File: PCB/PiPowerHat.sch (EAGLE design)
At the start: 48 parts, among them J3 Display, J4 FAN1, K1 PIN20X2, Q1 NX2301P, U1 EEPROM24, U2 INA219AIDCNRSOIC, U3 TSL2561T, U4 DS18B20, U5 DS1820SOIC, U6 74AC125

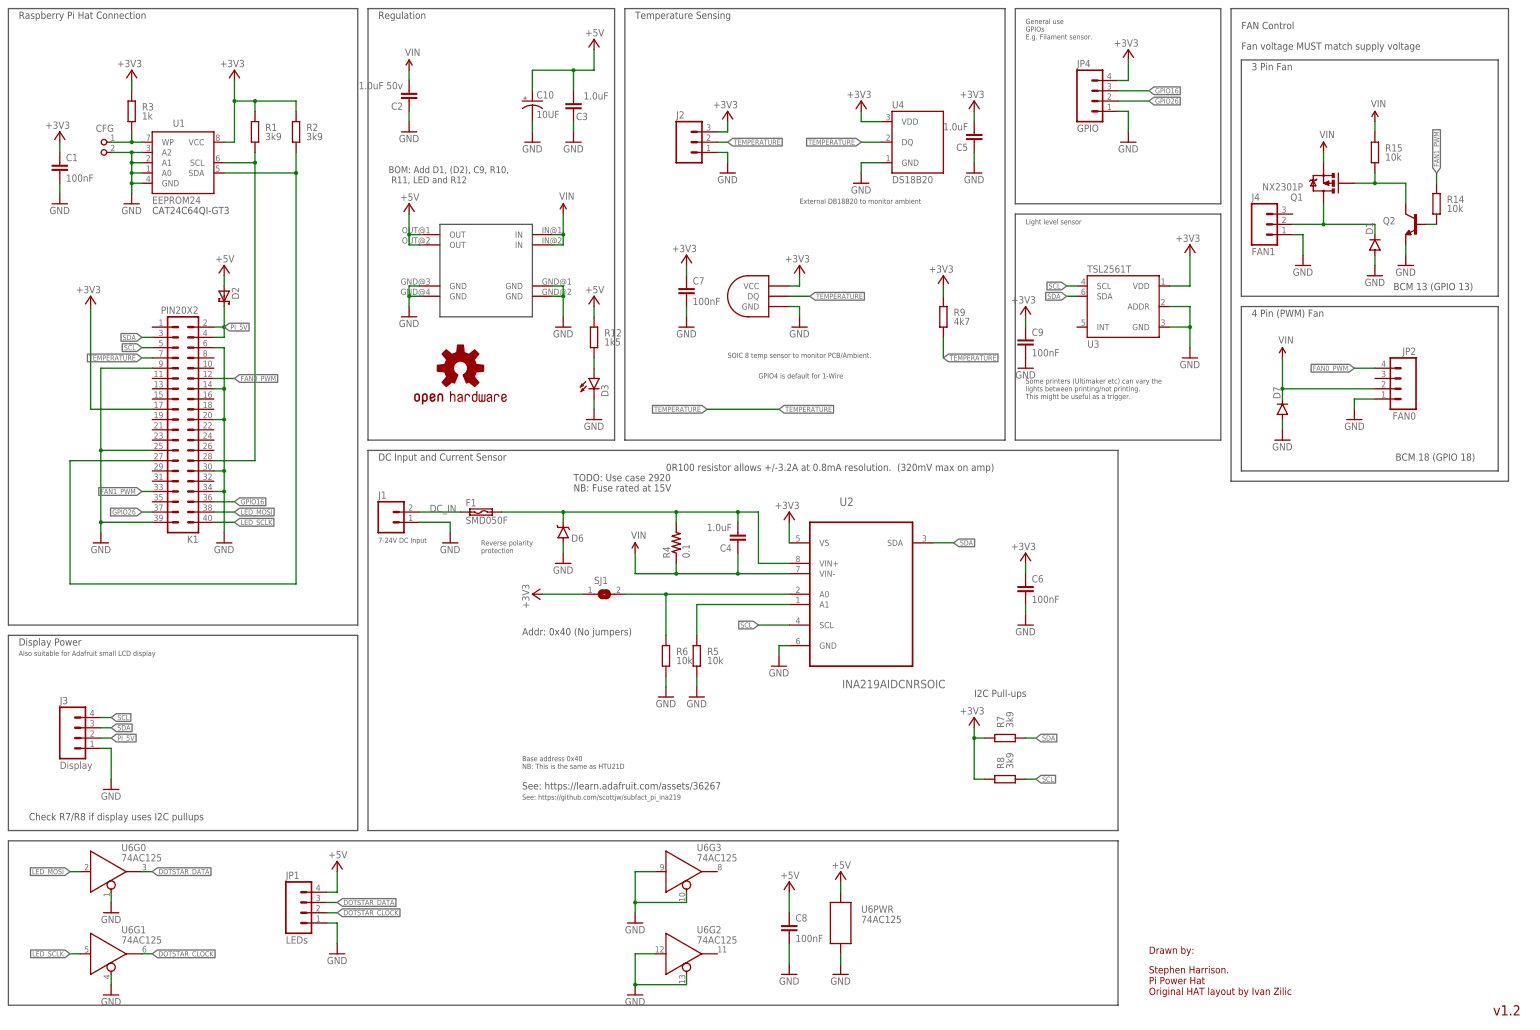
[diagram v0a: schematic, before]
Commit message: Update to rearrange the board a bit better.
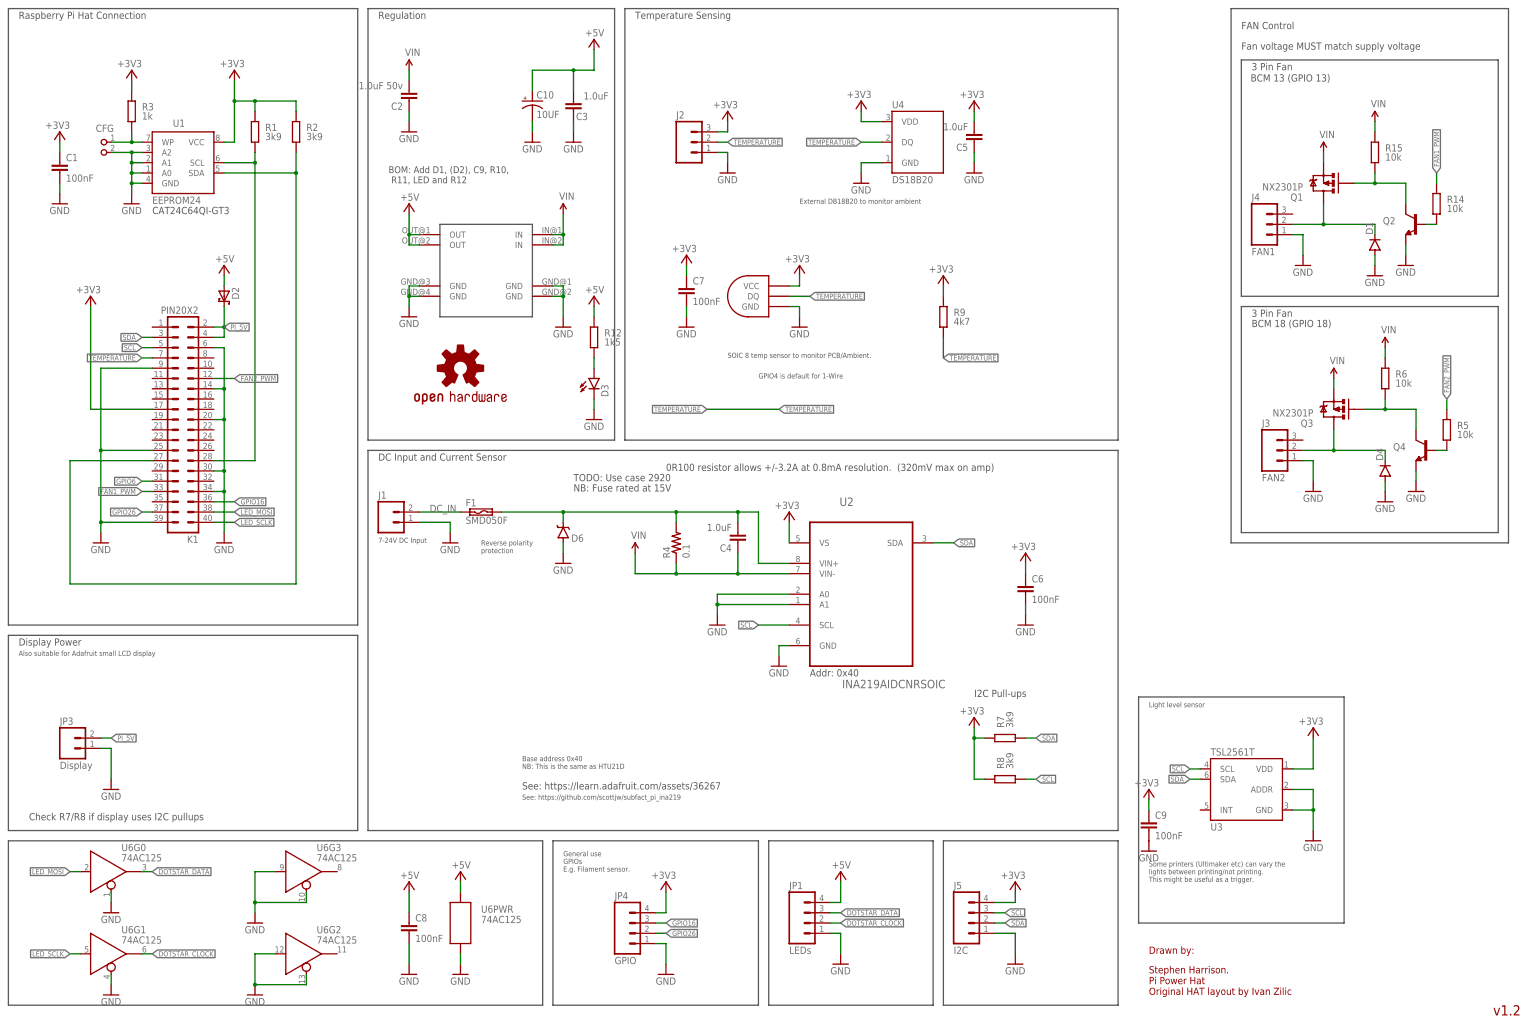
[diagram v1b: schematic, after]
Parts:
- removed D7: (no value), SparkFun-DiscreteSemi:DIODESOD123
- removed JP2: FAN0, SparkFun-Connectors:M04POLAR
- removed SJ1: (no value), jumper:SJ
- added D4: (no value), SparkFun-DiscreteSemi:DIODESOD123
- added J5: I2C, SparkFun-Connectors:M04POLAR
- added JP3: Display, SparkFun-Connectors:M02POLAR
- added Q3: NX2301P, SparkFun-DiscreteSemi:MOSFET-PCHANNEL
- added Q4: (no value), SparkFun-DiscreteSemi:TRANSISTOR_NPNSOT23-3
- J3: value Display -> FAN2; device SparkFun-Connectors:M04POLAR -> SparkFun-Connectors:M03POLAR
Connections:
- removed net FAN0_PWM: JP2.4, K1.12
- removed net N$10: R5.2, U2.A1
- removed net N$9: R6.2, SJ1.2, U2.A0
- new net FAN2_PWM: K1.12, R5.2
- new net GPIO6: K1.31
- new net N$1: D4.C, J3.2, Q3.D
- new net N$2: Q4.B, R5.1
- new net N$6: Q3.G, Q4.C, R6.1
- net +3V3: now also J5.4; no longer SJ1.1
- net GND: now also D4.A, J5.1, JP3.1, Q4.E, U2.A0, U2.A1; no longer D7.A, JP2.1, R5.1, R6.1
- net PI_5V: now also JP3.2; no longer J3.2
- net SCL: now also J5.3; no longer J3.4
- net SDA: now also J5.2; no longer J3.3
- net VIN: now also Q3.S, R6.2; no longer D7.C, JP2.2
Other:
- note added: "Addr: 0x40"
- note removed: "4 Pin (PWM) Fan"
- note removed: "Addr: 0x40 (No jumpers)"
- moved on the sheet: C8, C9, JP1, JP4, R5, R6, U3, U6G2, U6G3, U6PWR

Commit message: Removed 3v3/5V logic converter in favour of just a second 3v3 GPIO port.
Added Fan3 which is permenantly connected to the VIn supply to allow it to be used to power a fan or something else whilst still having current monitoring without the current restriction of the p-channel fets.

Slight improvements in routing.
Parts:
- removed C8: 100nF, resistor:C-EUC0805K
- removed U$1: MINI-BUCK-MODULE-3A, Tinamous:MINI-BUCK-MODULE-3A
- removed U6: 74AC125, SparkFun-DigitalIC:74AC125DG125
- added D5: (no value), SparkFun-DiscreteSemi:DIODESOD123
- added D7: (no value), SparkFun-LED:LED1206
- added J6: FAN3, SparkFun-Connectors:M03POLAR
- added R10: 1k5, resistor:R-EU_M0805
- added RG1: MINI-BUCK-MODULE-3A, Tinamous:MINI-BUCK-MODULE-3A
- JP1: value LEDs -> GPIO2
- JP4: value GPIO -> GPIO1
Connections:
- removed net DOTSTAR_CLOCK: JP1.2, U6G1.Q
- removed net DOTSTAR_DATA: JP1.3, U6G0.Q
- removed net GPIO6: K1.31
- removed net LED_MOSI: K1.38, U6G0.D
- removed net LED_SCLK: K1.40, U6G1.D
- new net GPIO11: K1.23, R10.2
- new net GPIO20: JP1.3, K1.38
- new net GPIO21: JP1.2, K1.40
- new net N$9: D7.A, R10.1
- net +3V3: now also JP1.4
- net +5V: now also RG1.OUT@1, RG1.OUT@2; no longer C8.1, JP1.4, U$1.OUT@1, U$1.OUT@2, U6PWR.P$V+
- net GND: now also D5.A, D7.C, J6.1, RG1.GND@1, RG1.GND@2, RG1.GND@3, RG1.GND@4; no longer C8.2, U$1.GND@1, U$1.GND@2, U$1.GND@3, U$1.GND@4, U6G0.!EN, U6G1.!EN, U6G2.!EN, U6G2.D, U6G3.!EN, U6G3.D, U6PWR.P$V-
- net VIN: now also D5.C, J6.2, RG1.IN@1, RG1.IN@2; no longer U$1.IN@1, U$1.IN@2
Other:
- note added: "Always powered. May be used to power to power other things from VIN and monitor current."
- note added: "Fan voltages MUST match supply voltage"
- note added: "v1.2.1"
- note removed: "BOM: Add D1, (D2), C9, R10, R11, LED and R12"
- note removed: "Check R7/R8 if display uses I2C pullups"
- note removed: "Fan voltage MUST match supply voltage"
- note removed: "v1.2"
- moved on the sheet: C2, C9, D1, D3, D4, J3, J4, J5, JP1, JP3, JP4, Q1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

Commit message: Updated silk screen. Sent to DirtyPCBs.
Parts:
- added C8: 10UF 35V, SparkFun-Capacitors:10UF-25V-10%(SMT-TANT)
- C10: value 10UF -> 100UF 10V
- F1: FARNELL-NEW (none) -> 1822225
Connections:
- net GND: now also C8.-
- net VIN: now also C8.+
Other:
- note added: "Alternative: MAX31820PARMCR+ (Farnell 2515556)"
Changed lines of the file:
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@@
 <part name="F1" library="switch-raychem" deviceset="SMD*F" device="" technology="050">
 <attribute name="FARNELL" value="1822231"/>
+<attribute name="FARNELL-NEW" value="1822225"/>
 </part>
 <part name="GND18" library="supply1" deviceset="GND" device=""/>
@@
 <part name="+3V17" library="supply1" deviceset="+3V3" device=""/>
 <part name="GND32" library="supply1" deviceset="GND" device=""/>
-<part name="C10" library="SparkFun-Capacitors" deviceset="10UF-25V-10%(SMT-TANT)" device="" value="10UF"/>
+<part name="C10" library="SparkFun-Capacitors" deviceset="10UF-25V-10%(SMT-TANT)" device="" value="100UF 10V"/>
 <part name="U3" library="SparkFun-Sensors" deviceset="TSL2561" device="T"/>
 <part name="+3V15" library="supply1" deviceset="+3V3" device=""/>
@@
 <part name="GND25" library="supply1" deviceset="GND" device=""/>
 <part name="D7" library="SparkFun-LED" deviceset="LED" device="1206"/>
+<part name="C8" library="SparkFun-Capacitors" deviceset="10UF-25V-10%(SMT-TANT)" device="" value="10UF 35V">
+<attribute name="FARNELL" value="197634"/>
+</part>
 </parts>
 <sheets>
@@
 <wire x1="208.28" y1="7.62" x2="165.1" y2="7.62" width="0.1524" layer="97"/>
 <wire x1="165.1" y1="7.62" x2="165.1" y2="48.26" width="0.1524" layer="97"/>
+<text x="203.2" y="203.2" size="1.27" layer="97">Alternative: MAX31820PARMCR+ (Farnell 2515556)</text>
 </plain>
 <instances>
@@
 <instance part="F1" gate="G$1" x="124.46" y="129.54">
 <attribute name="FARNELL" x="124.46" y="129.54" size="1.27" layer="96" display="off"/>
+<attribute name="FARNELL-NEW" x="124.46" y="129.54" size="1.27" layer="96" display="off"/>
 </instance>
 <instance part="GND18" gate="1" x="226.06" y="22.86"/>
@@
 <instance part="GND25" gate="1" x="147.32" y="12.7"/>
 <instance part="D7" gate="G$1" x="147.32" y="25.4"/>
+<instance part="C8" gate="G$1" x="124.46" y="213.36">
+<attribute name="FARNELL" x="124.46" y="213.36" size="1.27" layer="96" display="off"/>
+</instance>
 </instances>
 <busses>
@@
 <pinref part="GND4" gate="1" pin="GND"/>
 <wire x1="116.84" y1="208.28" x2="116.84" y2="205.74" width="0.1524" layer="91"/>
+<pinref part="C8" gate="G$1" pin="-"/>
+<wire x1="124.46" y1="208.28" x2="124.46" y2="205.74" width="0.1524" layer="91"/>
+<wire x1="124.46" y1="205.74" x2="116.84" y2="205.74" width="0.1524" layer="91"/>
+<junction x="116.84" y="205.74"/>
 </segment>
 <segment>
@@
 <wire x1="116.84" y1="215.9" x2="116.84" y2="218.44" width="0.1524" layer="91"/>
 <pinref part="SUPPLY1" gate="G$1" pin="VIN"/>
-</segment>
-<segment>
+<pinref part="C8" gate="G$1" pin="+"/>
+<wire x1="124.46" y1="215.9" x2="124.46" y2="218.44" width="0.1524" layer="91"/>
+<wire x1="124.46" y1="218.44" x2="116.84" y2="218.44" width="0.1524" layer="91"/>
+<junction x="116.84" y="218.44"/>
+</segment>
+<segment>
